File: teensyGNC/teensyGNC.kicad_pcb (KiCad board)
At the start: 4 copper layers, 53 x 139.5 mm, 46 parts, among them J1 ESC_1_PWM, J10 ToF_OF_SH, J11 Hall_1_PH, J12 Hall_2_PH, J13 Hall_3_PH, J14 Hall_4_PH, J2 5V_In_XH, J3 ESC_2_PWM, J4 Servo_1_PWM, J5 Servo_2_PWM, J6 7V4_In, J7 Ebyte, J8 LC29H, J9 Batt_Mon_GH, U1 E28-2G4T20SX, U2 4754, U3 AP2112K-3.3, U4 4494, U5 Teensy4.1

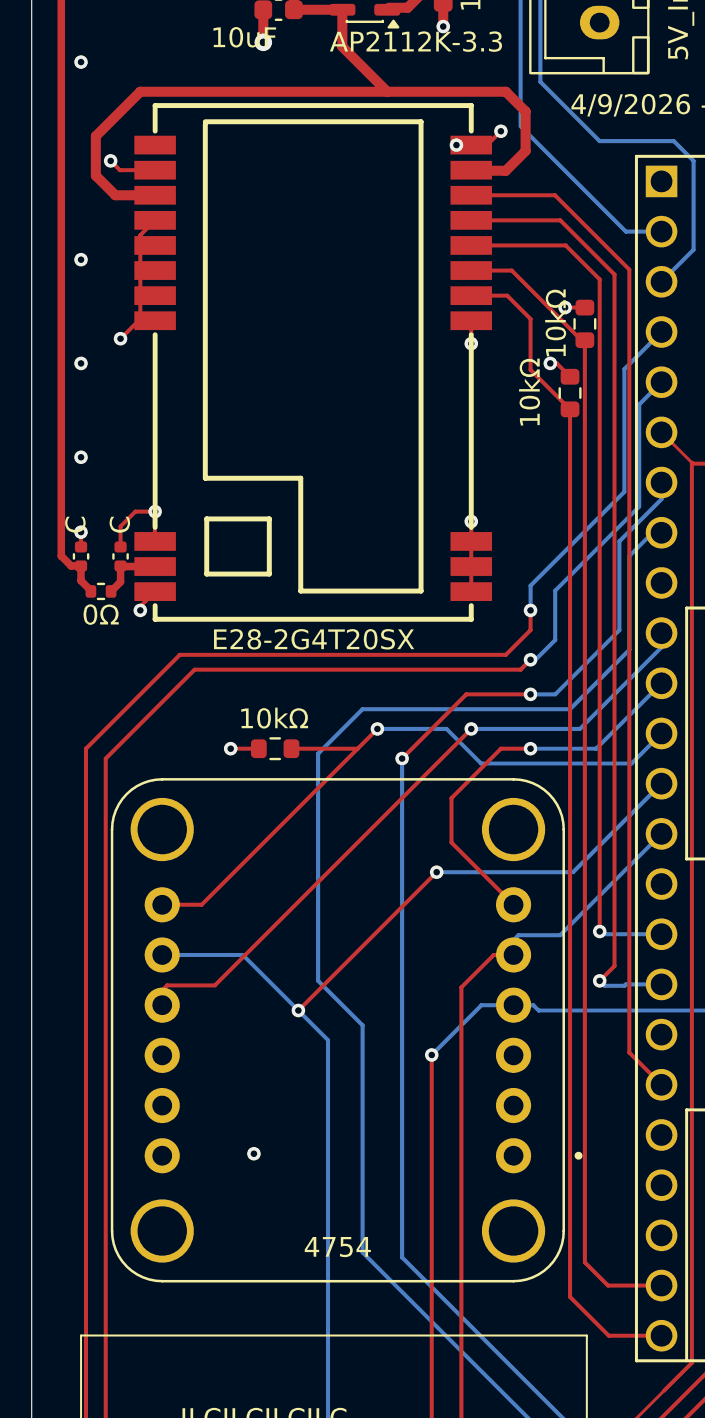
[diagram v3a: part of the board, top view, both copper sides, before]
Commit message: Small fixes
- DRC now runs OK for all three ground pours (shifted ebyte around a little bit closer to teensy)
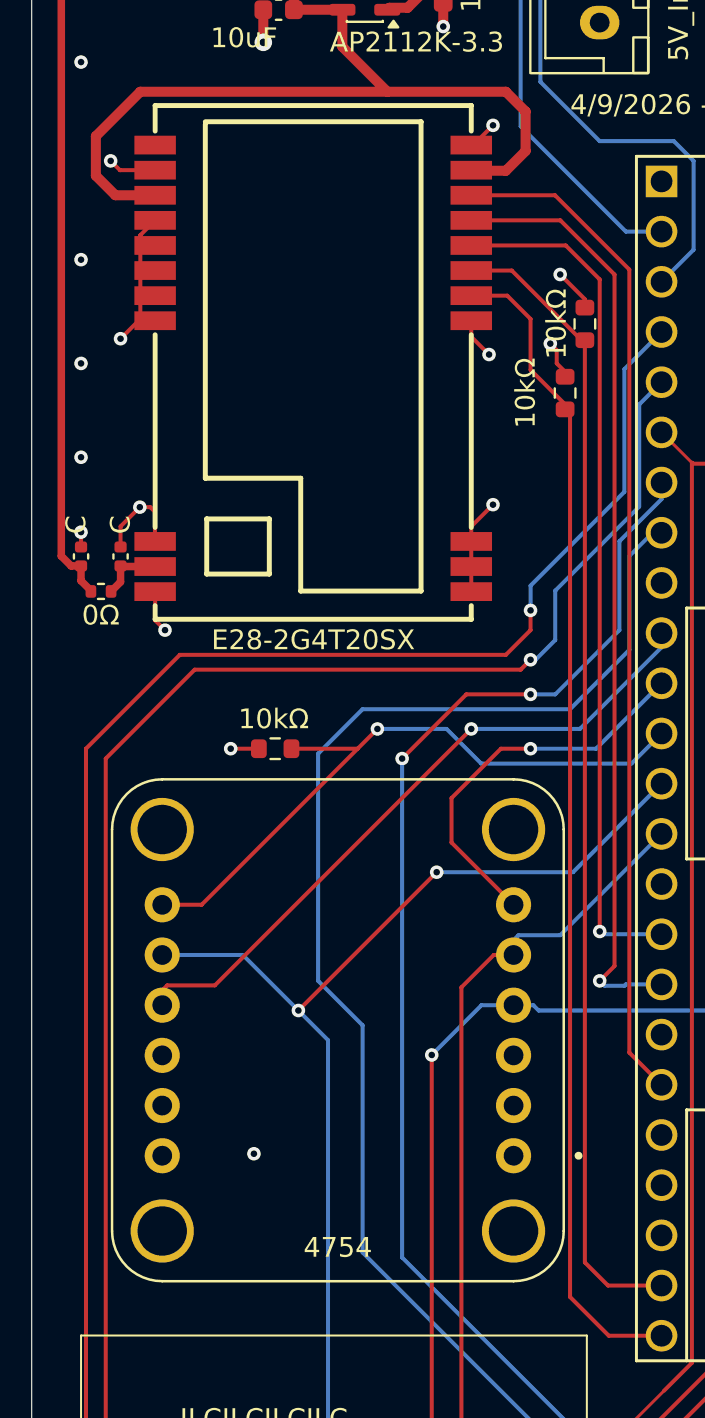
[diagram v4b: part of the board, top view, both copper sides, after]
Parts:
- moved R10 0.25 mm to (98.2, 72.8)
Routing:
- net GND: track 63.2 -> 68.1 mm, vias 47 -> 46
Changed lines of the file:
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@@
 		)
 		(embedded_fonts no)
+		(model "${KIPRJMOD}/4494.pretty/4494.step"
+			(hide yes)
+			(offset
+				(xyz 0 0 0)
+			)
+			(scale
+				(xyz 1 1 1)
+			)
+			(rotate
+				(xyz 0 0 0)
+			)
+		)
+		(model "C:/Users/Chris Cheang/Downloads/adafruit Adafruit_CAD_Parts main 4494 DPS310 Sensor/4494-DPS310-Sensor.step"
+			(offset
+				(xyz -12.7 -9 11)
+			)
+			(scale
+				(xyz 1 1 1)
+			)
+			(rotate
+				(xyz -0 -0 -0)
+			)
+		)
 	)
 	(footprint "MountingHole:MountingHole_3.2mm_M3"
@@
 	(footprint "Resistor_SMD:R_0603_1608Metric"
 		(layer "F.Cu")
-		(at 98.5 72.75 -90)
+		(at 98.25 72.75 -90)
 		(descr "Resistor SMD 0603 (1608 Metric), square (rectangular) end terminal, IPC-7351 nominal, (Body size source: IPC-SM-782 page 72, https://www.pcb-3d.com/wordpress/wp-content/uploads/ipc-sm-782a_amendment_1_and_2.pdf)")
 		(tags "resistor")
@@
 	)
 	(segment
-		(start 76.75 83.55)
-		(end 76.75 83.75)
-		(width 0.2032)
-		(layer "F.Cu")
-		(net "GND")
-	)
-	(segment
-		(start 97.5 71.25)
-		(end 97.825 71.25)
-		(width 0.2032)
-		(layer "F.Cu")
-		(net "GND")
-	)
-	(segment
 		(start 111 152.25)
 		(end 110.75 152.25)
@@
 	)
 	(segment
-		(start 99.25 68.425)
-		(end 98.25 68.425)
+		(start 99.25 68)
+		(end 98 66.75)
 		(width 0.2032)
 		(layer "F.Cu")
@@
 	)
 	(segment
-		(start 77.49 80.25)
-		(end 77.5 80.26)
-		(width 0.2032)
+		(start 92.08125 53)
+		(end 92.08125 54.2)
+		(width 0.508)
 		(layer "F.Cu")
 		(net "GND")
 	)
 	(segment
-		(start 93.5 79.25)
-		(end 93.5 82.8)
-		(width 0.2032)
+		(start 109.85 151.35)
+		(end 109.85 150.75)
+		(width 0.508)
 		(layer "F.Cu")
 		(net "GND")
 	)
 	(segment
-		(start 76.5 78.75)
-		(end 75.75 79.5)
+		(start 93.5 79.5)
+		(end 93.5 82.8)
 		(width 0.2032)
 		(layer "F.Cu")
@@
 	)
 	(segment
-		(start 92.08125 53)
-		(end 92.08125 54.2)
-		(width 0.508)
-		(layer "F.Cu")
-		(net "GND")
-	)
-	(segment
-		(start 109.85 151.35)
-		(end 109.85 150.75)
-		(width 0.508)
+		(start 93.7 60.1)
+		(end 93.6 60.1)
+		(width 0.2032)
 		(layer "F.Cu")
 		(net "GND")
@@
 	)
 	(segment
-		(start 77.5 78.75)
-		(end 77.49 78.76)
-		(width 0.2032)
-		(layer "F.Cu")
-		(net "GND")
-	)
-	(segment
-		(start 77.5 78.75)
-		(end 76.5 78.75)
+		(start 97.825 70.575)
+		(end 97.825 71.25)
 		(width 0.2032)
 		(layer "F.Cu")
@@
 	)
 	(segment
+		(start 77.5 84.25)
+		(end 77.5 82.8)
+		(width 0.2032)
+		(layer "F.Cu")
+		(net "GND")
+	)
+	(segment
 		(start 108 139.25)
 		(end 110.75 136.5)
@@
 	)
 	(segment
-		(start 95 59.5)
-		(end 94.3 60.2)
+		(start 77.49 78.76)
+		(end 77.49 80.25)
 		(width 0.2032)
 		(layer "F.Cu")
@@
 	)
 	(segment
-		(start 75.72 61.47)
-		(end 77.5 61.47)
+		(start 98.25 71.675)
+		(end 98.25 71.925)
 		(width 0.2032)
 		(layer "F.Cu")
@@
 	)
 	(segment
-		(start 109.25 156.75)
-		(end 107.85 156.75)
-		(width 0.508)
-		(layer "F.Cu")
-		(net "GND")
-	)
-	(segment
-		(start 75.75 79.5)
-		(end 75.75 80.54)
+		(start 75.72 61.47)
+		(end 77.5 61.47)
 		(width 0.2032)
 		(layer "F.Cu")
@@
 	)
 	(segment
-		(start 94.3 60.2)
-		(end 93.5 60.2)
-		(width 0.2032)
+		(start 109.25 156.75)
+		(end 107.85 156.75)
+		(width 0.508)
 		(layer "F.Cu")
 		(net "GND")
@@
 	)
 	(segment
+		(start 77.49 80.25)
+		(end 77.5 80.26)
+		(width 0.2032)
+		(layer "F.Cu")
+		(net "GND")
+	)
+	(segment
 		(start 109.85 150.4)
 		(end 109.85 150.75)
@@
 	)
 	(segment
-		(start 77.49 78.76)
-		(end 77.49 80.25)
-		(width 0.2032)
-		(layer "F.Cu")
-		(net "GND")
-	)
-	(segment
-		(start 77.5 82.8)
-		(end 76.75 83.55)
+		(start 77.255 78.525)
+		(end 77.49 78.76)
 		(width 0.2032)
 		(layer "F.Cu")
@@
 	)
 	(segment
-		(start 93.5 70.25)
-		(end 93.5 69.09)
+		(start 76.725 78.525)
+		(end 77.255 78.525)
 		(width 0.2032)
 		(layer "F.Cu")
@@
 	)
 	(segment
+		(start 78 84.75)
+		(end 77.5 84.25)
+		(width 0.2032)
+		(layer "F.Cu")
+		(net "GND")
+	)
+	(segment
+		(start 76.725 78.525)
+		(end 75.75 79.5)
+		(width 0.2032)
+		(layer "F.Cu")
+		(net "GND")
+	)
+	(segment
 		(start 108 145.25)
 		(end 109.5 143.75)
@@
 	)
 	(segment
+		(start 93.5 69.9)
+		(end 93.5 69.09)
+		(width 0.2032)
+		(layer "F.Cu")
+		(net "GND")
+	)
+	(segment
+		(start 75.75 79.5)
+		(end 75.75 80.54)
+		(width 0.2032)
+		(layer "F.Cu")
+		(net "GND")
+	)
+	(segment
 		(start 107.75 142.25)
 		(end 108 142.25)
@@
 	)
 	(segment
+		(start 94.6 78.4)
+		(end 93.5 79.5)
+		(width 0.2032)
+		(layer "F.Cu")
+		(net "GND")
+	)
+	(segment
+		(start 99.25 68.425)
+		(end 99.25 68)
+		(width 0.2032)
+		(layer "F.Cu")
+		(net "GND")
+	)
+	(segment
+		(start 94.6 59.2)
+		(end 93.7 60.1)
+		(width 0.2032)
+		(layer "F.Cu")
+		(net "GND")
+	)
+	(segment
+		(start 97.5 70.25)
+		(end 97.825 70.575)
+		(width 0.2032)
+		(layer "F.Cu")
+		(net "GND")
+	)
+	(segment
 		(start 110.875 149.375)
 		(end 109.85 150.4)
@@
 	)
 	(segment
+		(start 94.4 70.8)
+		(end 93.5 69.9)
+		(width 0.2032)
+		(layer "F.Cu")
+		(net "GND")
+	)
+	(segment
 		(start 73.75 79.79)
 		(end 73.75 80.54)
@@
 	)
 	(segment
+		(start 97.825 71.25)
+		(end 98.25 71.675)
+		(width 0.2032)
+		(layer "F.Cu")
+		(net "GND")
+	)
+	(segment
 		(start 120.75 151.25)
 		(end 120.75 150.75)
@@
 	)
 	(segment
-		(start 97.825 71.25)
-		(end 98.5 71.925)
+		(start 93.6 60.1)
+		(end 93.5 60.2)
 		(width 0.2032)
 		(layer "F.Cu")
@@
 	)
 	(via
-		(at 98.25 68.425)
-		(size 0.6858)
-		(drill 0.3302)
-		(layers "F.Cu" "B.Cu")
-		(net "GND")
-	)
-	(via
-		(at 92.75 60.2)
+		(at 98 66.75)
 		(size 0.6858)
 		(drill 0.3302)
@@
 	)
 	(via
-		(at 95 59.5)
+		(at 94.6 59.2)
 		(size 0.6858)
 		(drill 0.3302)
@@
 	)
 	(via
-		(at 93.5 70.25)
+		(at 94.4 70.8)
 		(size 0.6858)
 		(drill 0.3302)
@@
 	)
 	(via
-		(at 76.75 83.75)
+		(at 78 84.75)
 		(size 0.6858)
 		(drill 0.3302)
@@
 	)
 	(via
-		(at 77.5 78.75)
+		(at 76.725 78.525)
 		(size 0.6858)
 		(drill 0.3302)
@@
 	)
 	(via
-		(at 93.5 79.25)
+		(at 94.6 78.4)
 		(size 0.6858)
 		(drill 0.3302)
@@
 	)
 	(via
-		(at 97.5 71.25)
+		(at 97.5 70.25)
 		(size 0.6858)
 		(drill 0.3302)
@@
 	)
 	(segment
+		(start 98.5 73.825)
+		(end 98.5 118.5)
+		(width 0.2032)
+		(layer "F.Cu")
+		(net "Net-(U1-M0)")
+	)
+	(segment
 		(start 95.32 67.82)
 		(end 93.5 67.82)
@@
 	)
 	(segment
-		(start 96.5 71.575)
-		(end 96.5 69)
+		(start 96.5 69)
+		(end 95.32 67.82)
 		(width 0.2032)
 		(layer "F.Cu")
@@
 	)
 	(segment
-		(start 98.5 73.575)
-		(end 98.5 118.5)
+		(start 98.5 118.5)
+		(end 100.46 120.46)
 		(width 0.2032)
 		(layer "F.Cu")
@@
 	)
 	(segment
-		(start 100.46 120.46)
-		(end 103.13 120.46)
+		(start 98.25 73.575)
+		(end 98.5 73.825)
 		(width 0.2032)
 		(layer "F.Cu")
@@
 	)
 	(segment
-		(start 96.5 69)
-		(end 95.32 67.82)
+		(start 98.25 73.575)
+		(end 98.25 73.325)
+		(width 0.2032)
+		(layer "F.Cu")
+		(net "Net-(U1-M0)")
+	)
+	(segment
+		(start 96.5 71.575)
+		(end 96.5 69)
 		(width 0.2032)
 		(layer "F.Cu")
@@
 	)
 	(segment
-		(start 98.5 73.575)
+		(start 98.25 73.325)
 		(end 96.5 71.575)
 		(width 0.2032)
@@
 	)
 	(segment
-		(start 98.5 118.5)
-		(end 100.46 120.46)
+		(start 100.46 120.46)
+		(end 103.13 120.46)
 		(width 0.2032)
 		(layer "F.Cu")

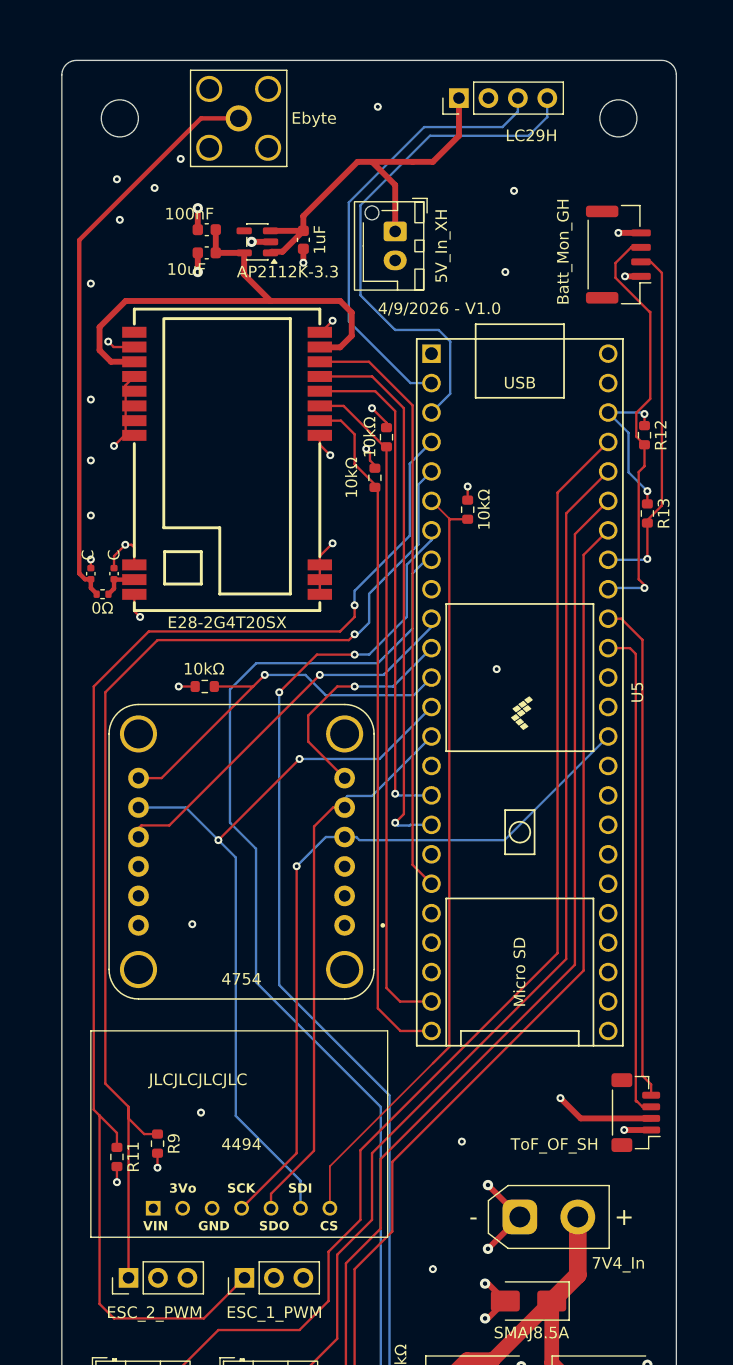
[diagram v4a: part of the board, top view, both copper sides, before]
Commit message: DRC passed and offboard connector pinouts checked
- All connectors vertical now for better cable management
- LCSC numbers added as fields for jlcpcb assembly
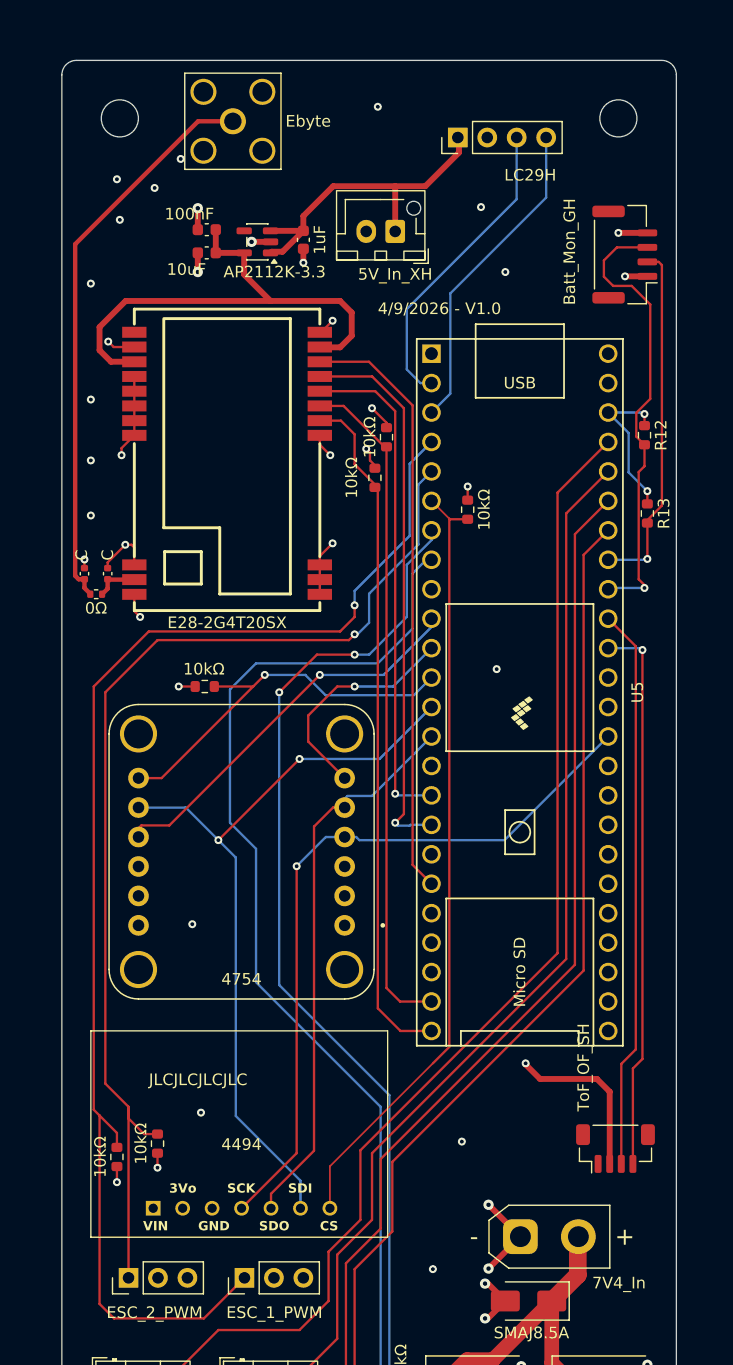
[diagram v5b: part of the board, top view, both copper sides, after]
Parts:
- moved J10 3.56 mm to (119.0, 130.6), turned to 0 degrees
- moved J8 3.40 mm to (105.4, 43.4)
- moved J6 1.70 mm to (110.8, 138.2)
- moved J7 0.56 mm to (86.0, 42.0)
- moved R4 0.55 mm to (74.2, 82.8)
- moved C5 0.55 mm to (75.2, 81.0)
- moved C6 0.55 mm to (73.2, 81.0)
- moved J9 0.55 mm to (119.8, 53.5)
- turned J2 to 180 degrees
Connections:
- U5 pad 38: Net-(J10-Pin_3) -> Net-(J10-Pin_4)
- U5 pad 39: Net-(J10-Pin_4) -> Net-(J10-Pin_3)
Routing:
- net Net-(J8-Pin_4): track 44.9 -> 27.8 mm
- net Net-(J8-Pin_3): track 38.6 -> 26.5 mm
- net Net-(J10-Pin_3): track 42.7 -> 48.5 mm
- net Net-(J10-Pin_4): track 43.3 -> 47.7 mm, vias 0 -> 1
- net +5V: track 143.1 -> 140.0 mm
- net Net-(J9-Pin_3): track 36.4 -> 39.4 mm
- net +7.4V: track 52.0 -> 50.3 mm
- net GND: track 68.1 -> 67.1 mm, vias 46 -> 45
- net Net-(U1-ANT): track 3.25 -> 3.80 mm
- net Net-(J7-In): track 49.6 -> 49.0 mm

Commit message: Test fabrication
- Downloaded fabrication toolkit
- Updated LCSC Part --> LCSC Part #
- Test BOM and gerber creation using toolkit
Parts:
- C5, C6: footprint Capacitor_SMD:C_0402_1005Metric -> Capacitor_SMD:C_0603_1608Metric
- R4: footprint Resistor_SMD:R_0402_1005Metric -> Resistor_SMD:R_0603_1608Metric
- moved C6 2.77 mm to (73.6, 78.3)
- moved C5 2.74 mm to (75.2, 78.3)
- moved R4 1.30 mm to (74.4, 81.5)
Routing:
- net Net-(U1-ANT): track 3.80 -> 4.94 mm
- net Net-(J7-In): track 49.0 -> 49.9 mm
- net GND: track 67.1 -> 67.6 mm, vias 45 -> 44
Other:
- board text added: "5/9/2026 - V1.0"
- board text removed: "4/9/2026 - V1.0"

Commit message: First export sent to taobao JLCPCB for quoting + other stuff
- Text labels added for components and connectors
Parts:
- moved J3 1.57 mm to (76.4, 143.2)
- moved J1 1.45 mm to (87.0, 143.2)
- moved J5 0.96 mm to (113.8, 162.2)
- moved J4 0.95 mm to (102.8, 162.2)
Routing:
- net Net-(U5-6_OUT1D): track 120.7 -> 113.0 mm, vias 1 -> 2
- net +3V3: track 18.4 -> 16.3 mm
- net +7.4V: track 50.3 -> 52.2 mm
- net Net-(J3-Pin_1): track 95.9 -> 97.6 mm
- net Net-(J11-Pin_3): track 101.0 -> 102.5 mm
- net Net-(J1-Pin_1): track 114.1 -> 115.6 mm
- net Net-(J9-Pin_3): track 39.4 -> 38.1 mm
- net Net-(J5-Pin_1): track 3.41 -> 4.42 mm
- net Net-(J4-Pin_1): track 4.97 -> 5.92 mm
- net Net-(J9-Pin_2): track 30.6 -> 30.1 mm
